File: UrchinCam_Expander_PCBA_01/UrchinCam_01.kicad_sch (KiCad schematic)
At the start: 90 parts, among them J1 95157-440LF, J2 SM04B-GHS, J3 SM04B-GHS, J4 SM02B-GHS, J5 SM04B-GHS, U1 MP6550, U2 ADS1115IDGS, U3 BNO085, U4 TSR3-2450N, U5 RTL8152B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

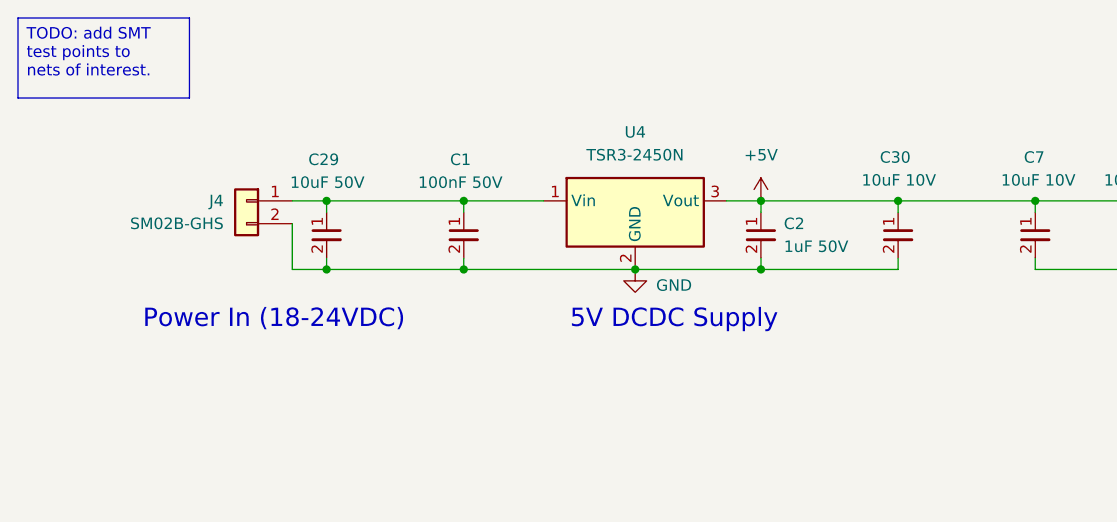
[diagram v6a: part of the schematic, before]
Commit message: Adding DCDC model.
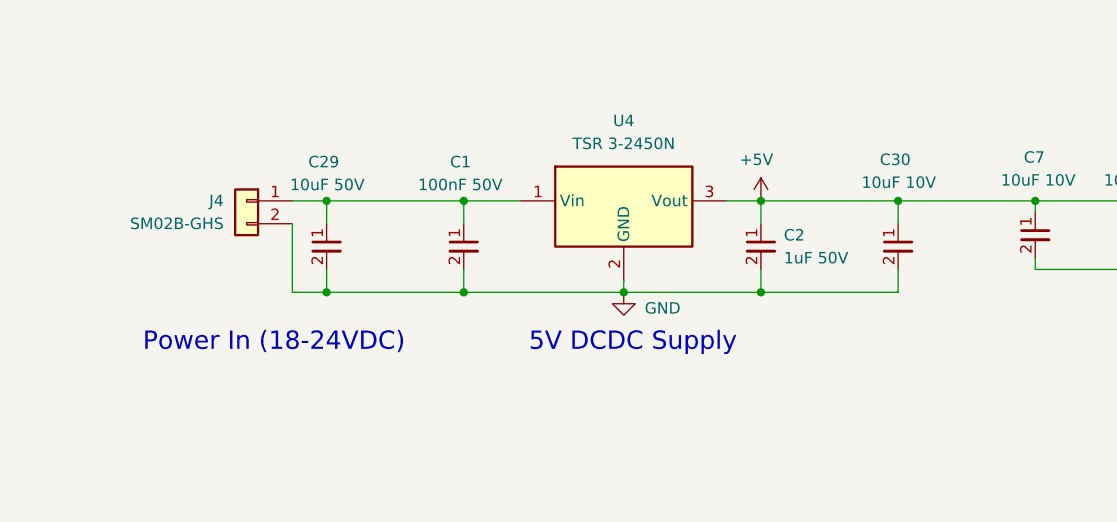
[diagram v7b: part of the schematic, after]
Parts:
- removed U4: TSR3-2450N, Converter_DCDC:Converter_DCDC_TRACO_TSR2-24xxN_TSR2-24xxxN_THT, symbol Regulator_Switching:TSR3-2450N
- added U4: TSR 3-2450N, DCDC_Converters:Traco_TSR 3-2450N, symbol DCDC_Converters:TSR_3-2450N
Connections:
- net +5V: now also U4.3 (Vout)
- net GND: now also U4.2 (GND)
- net at C1.1, C29.1, J4.1 (Pin_1): now also U4.1 (Vin)
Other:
- moved on the sheet: C1, C2, C29, C30

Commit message: Incorporated feedback from meeting.
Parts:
- added FID1, FID2, FID3, FID4: Fiducial, Fiducial:Fiducial_0.5mm_Mask1mm, symbol Mechanical:Fiducial
- added J6: SM02B-GHS, Connector_JST:JST_GH_SM02B-GHS-TB_1x02-1MP_P1.25mm_Horizontal, symbol Connectors:SM02B-GHS
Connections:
- net +5V: now also J6.1 (Pin_1)
- net GND: now also J6.2 (Pin_2)
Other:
- note added: "5V connection (alternate power source - external battery)"
- note added: "Fiducials"
- note added: "Power In (6.5 - 36 VDC)"
- note removed: "Power In (18-24VDC)"
- moved on the sheet: H1, H2, H3, H4, TP2, TP3, TP4
